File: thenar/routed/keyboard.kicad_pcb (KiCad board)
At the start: 2 copper layers, 137.3 x 110.9 mm, 81 parts, among them J1 Jumper, J2 Jumper, J3 Jumper, J4 Jumper, J5 Jumper, J6 Jumper

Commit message: feat(autoroute): use Global+Sequential strategy
freerouting defaults (Greedy+Prioritized) plateau quickly. Switching to
Global+Sequential produces identical final results but with cleaner
behavior - no NullPointerException warnings on first-pass attempts, and
freerouting actually completes the requested pass count instead of
bailing early on score-improvement heuristics.

This does NOT solve the underlying autoroute problem: the design still
has ~28 unrouted items after a 30-pass run. Those items are in the
dense areas (col4 matrix across the whole board, scrollwheel encoder
to jumper short hops, slider switch power nets) where freerouting's
greedy local optimization can't find routes that a human could.
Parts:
- removed the ? at (115.1, 87.2) (x2)
- removed the ? at (106.1, 136.2) (x2)
- added ? (x2): , lib:text, F.Cu at (115.1, 87.2)
- added ? (x2): , lib:text, F.Cu at (106.1, 136.2)

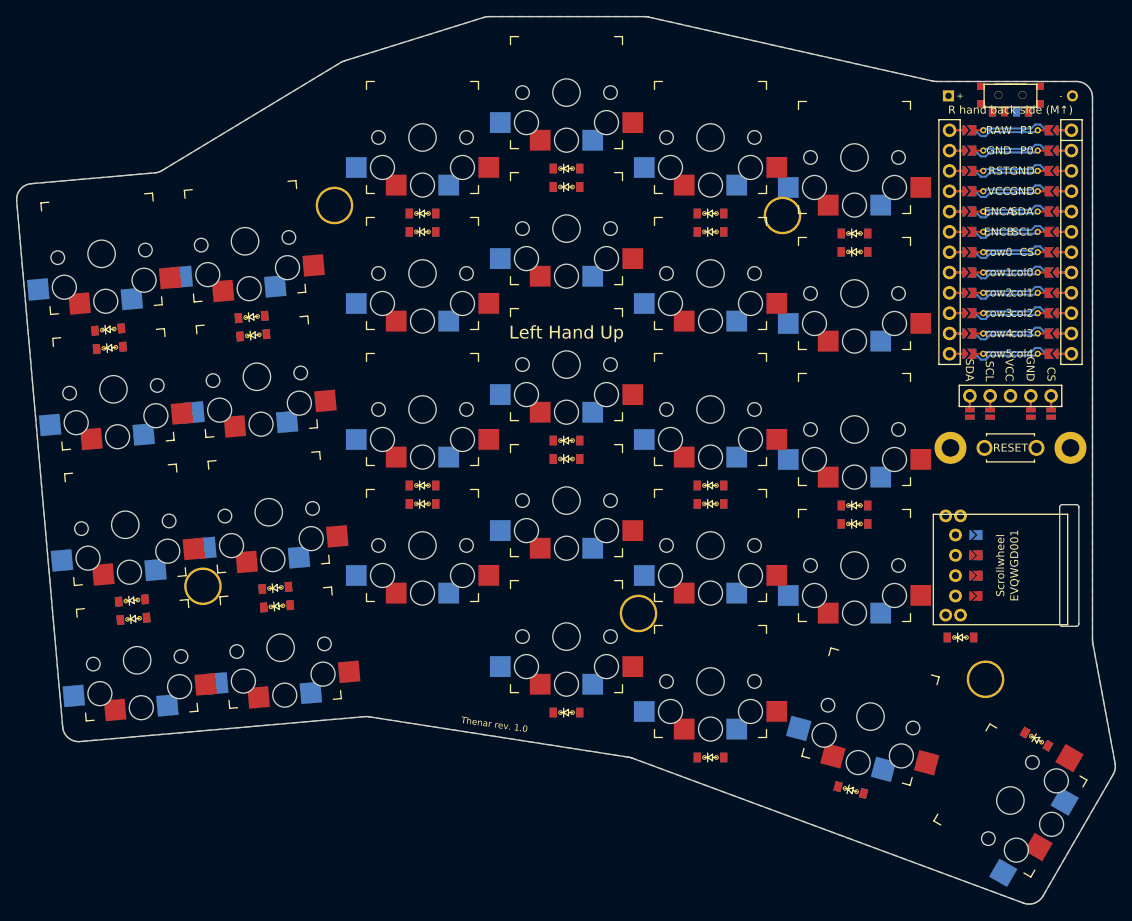
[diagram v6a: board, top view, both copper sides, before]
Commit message: pcb: hand-route the keyboard
DRC: 0 unconnected items. Remaining DRC warnings are all pre-existing
cosmetic issues from the upstream corax design (silk-over-copper from
labels under the Nice!Nano body, solder-mask-bridge between adjacent
LED/diode pads, intentionally-tight 0.1527mm clearance between solder
jumper bridge pads on J1-J6, one stray screw-hole/switch-pad overlap
on S26 from the original layout).

Routing took ~all 293 nets from scratch on the freshly-generated
scaffold (ceoloide footprints had already laid 200 internal traces for
the Nice!Nano/Nice!View reversibility jumpers, so the matrix + signal
routing was the rest).
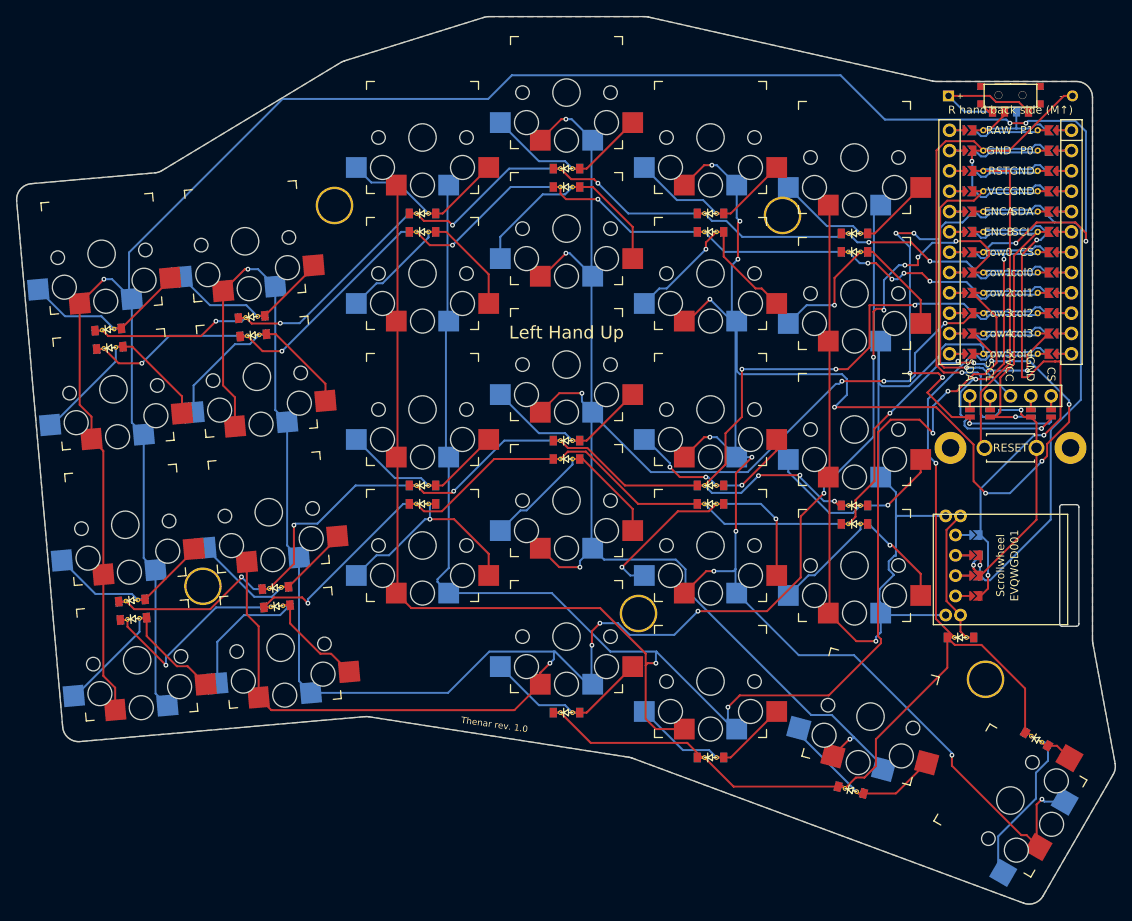
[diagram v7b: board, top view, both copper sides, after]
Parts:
- removed the ? at (115.1, 87.2) (x2)
- removed the ? at (106.1, 136.2) (x2)
- added ? (x2): , lib:text, F.Cu at (106.1, 136.2)
- added ? (x2): , lib:text, F.Cu at (115.1, 87.2)
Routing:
- net row0: track 9.84 -> 291.5 mm, vias 0 -> 5
- net row2: track 9.84 -> 291.4 mm, vias 0 -> 4
- net row1: track 9.84 -> 286.2 mm, vias 0 -> 11
- net row4: track 9.84 -> 243.9 mm, vias 0 -> 15
- net row3: track 9.84 -> 210.6 mm, vias 0 -> 8
- net col2: track 9.83 -> 179.2 mm, vias 0 -> 9
- net col3: track 9.83 -> 170.2 mm, vias 0 -> 6
- net row5: track 9.84 -> 163.8 mm, vias 0 -> 1
- net col1: track 9.83 -> 145.5 mm, vias 0 -> 8
- net col0: track 9.83 -> 142.8 mm, vias 0 -> 6
- net col4: track 9.83 -> 139.1 mm, vias 0 -> 1
- net GND: track 29.5 -> 127.0 mm, vias 0 -> 4
- net ENCB: track 9.84 -> 70.3 mm, vias 0 -> 3
- net ENCA: track 9.84 -> 67.8 mm, vias 0 -> 1
- net SDA: track 9.83 -> 65.5 mm, vias 0 -> 5
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
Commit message: pcb: re-route from autoroute baseline -- 44 vias (was 102)
Restarting from the freerouting v2.2.4 autoroute output and finishing
the ~25 unrouted nets by hand. Net result vs the from-scratch hand
route: same 0 unconnected items, ~2% longer total trace length, but
less than half the vias.

DRC: 0 unconnected. Remaining warnings are the same pre-existing
cosmetic issues from the upstream design (silk-over-copper, the
intentional 0.1527mm solder bridge clearance on J1-J6, one stray
screw-hole overlap on S26).

Drift check currently produces a false-positive (floating-point
precision noise from the SES roundtrip vs ergogen output - sub-micron
differences). To be addressed in a follow-up.
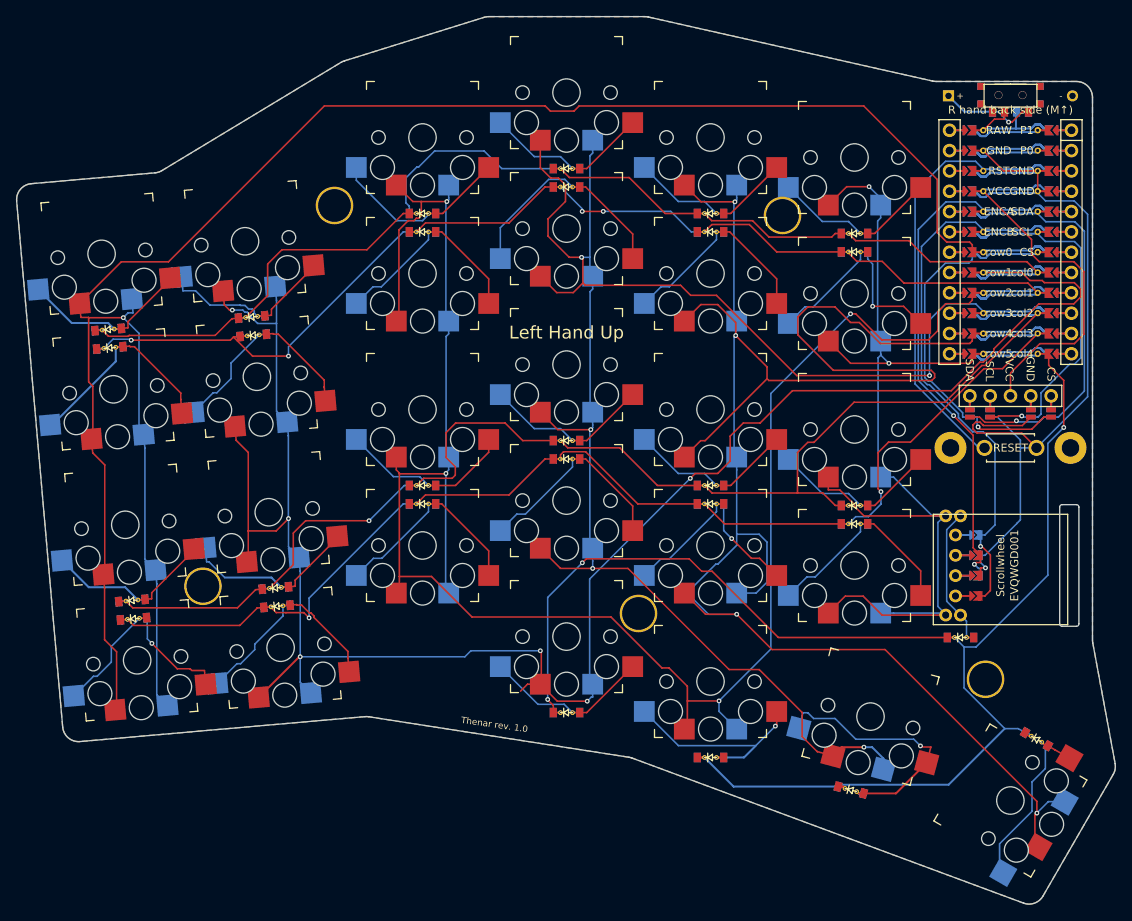
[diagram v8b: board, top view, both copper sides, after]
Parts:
- removed the ? at (106.1, 136.2) (x2)
- removed the ? at (115.1, 87.2) (x2)
- added ? (x2): , lib:text, F.Cu at (106.1, 136.2)
- added ? (x2): , lib:text, F.Cu at (115.1, 87.2)
- turned _8 to 23 degrees
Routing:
- net col4: track 139.1 -> 196.7 mm, vias 1 -> 3
- net row2: track 291.4 -> 247.3 mm
- net row0: track 291.5 -> 262.5 mm, vias 5 -> 1
- net row1: track 286.2 -> 260.6 mm, vias 11 -> 6
- net row3: track 210.6 -> 230.1 mm, vias 8 -> 5
- net col0: track 142.8 -> 160.7 mm, vias 6 -> 0
- net row4: track 243.9 -> 260.7 mm, vias 15 -> 4
- net row5: track 163.8 -> 147.2 mm, vias 1 -> 2
- net GND: track 127.0 -> 143.5 mm, vias 4 -> 1
- net RST: track 49.5 -> 63.3 mm
- net col1: track 145.5 -> 159.0 mm, vias 8 -> 4
- net SCL: track 40.9 -> 52.3 mm
- net layer_cluster: track 22.3 -> 33.2 mm, vias 0 -> 1
- net SDA: track 65.5 -> 57.8 mm, vias 5 -> 1
- net index_bottom: track 34.5 -> 27.4 mm, vias 2 -> 1
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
